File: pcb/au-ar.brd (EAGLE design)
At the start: 65 x 45 mm, 57 parts, among them U1 TPD12S016PWR, U2 TPD12S016PWR

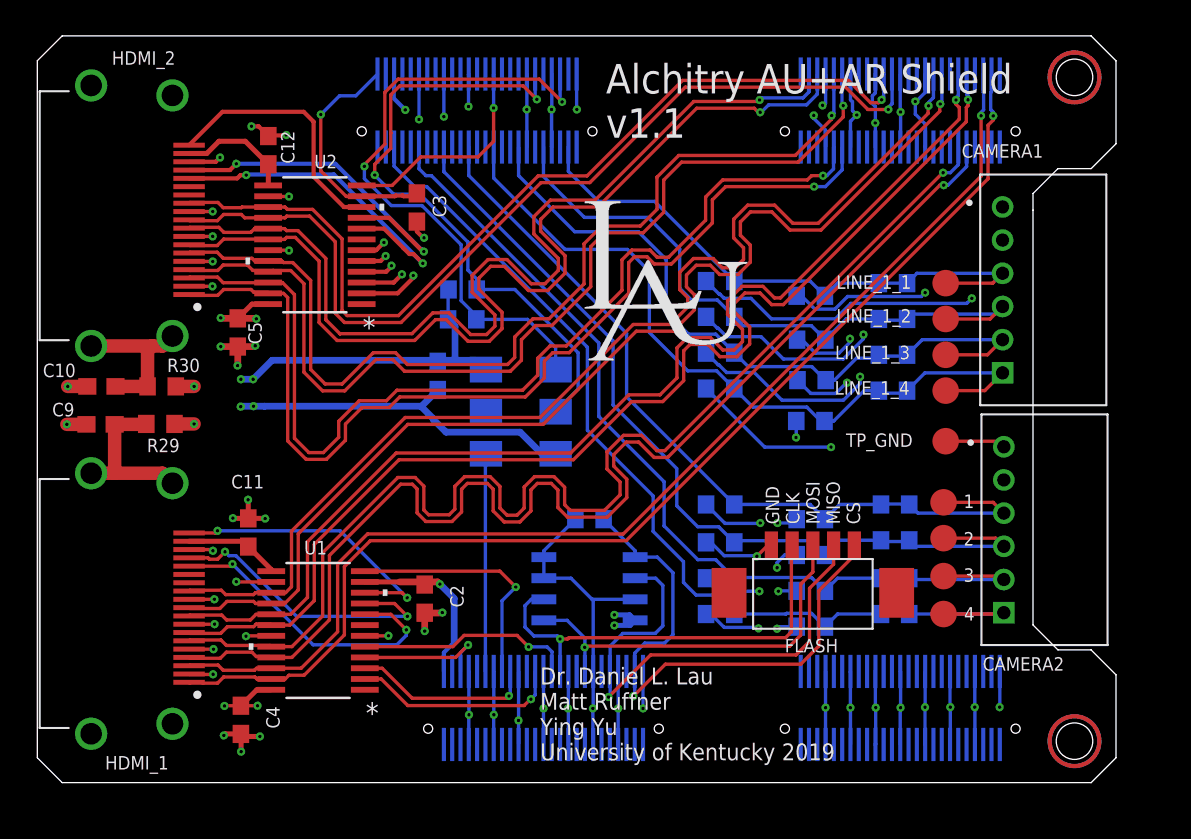
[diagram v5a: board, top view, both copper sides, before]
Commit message: retuned hdmi trace lengths, added ground pour and cutouts under hdmi connectors
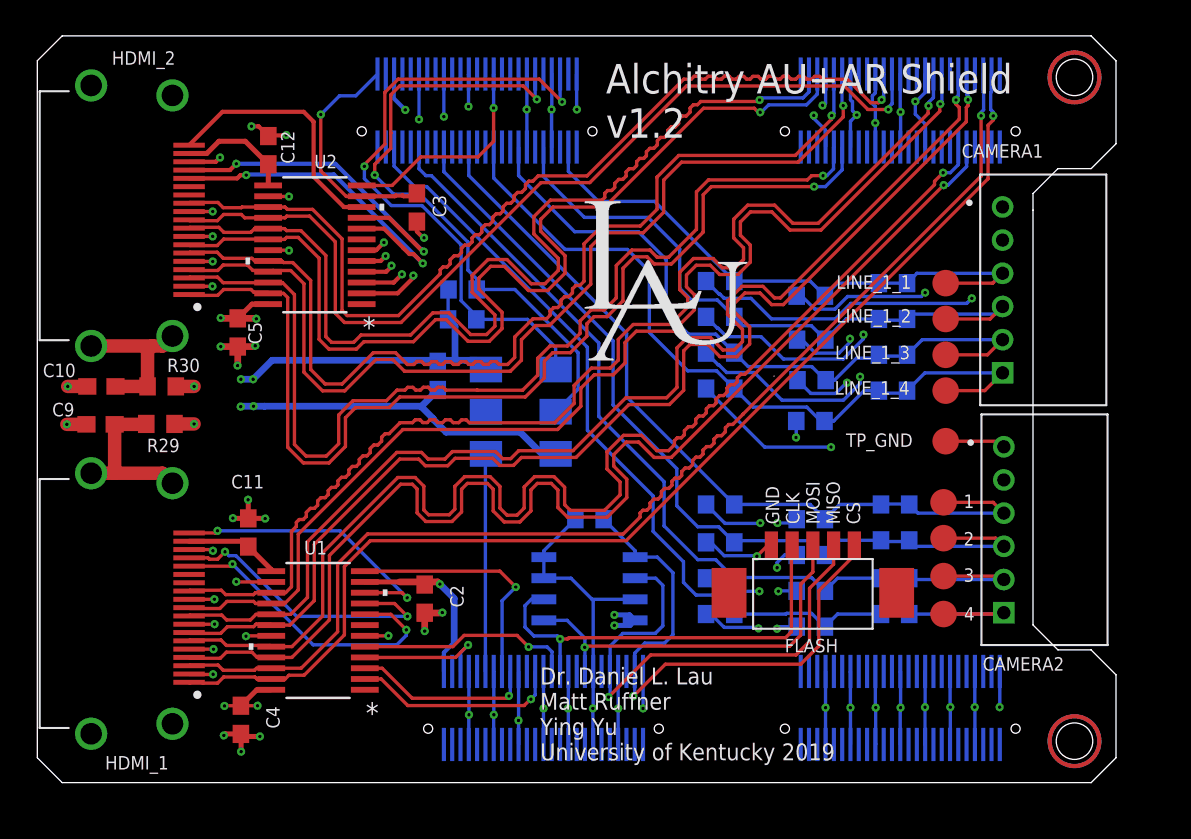
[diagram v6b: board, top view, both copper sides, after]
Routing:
- net CLK1_N: track 66.7 -> 70.0 mm
- net CLK2_N: track 55.3 -> 57.9 mm
- net D02_N: track 59.5 -> 61.9 mm
- net D22_N: track 60.1 -> 62.4 mm
- net D22_P: track 60.8 -> 62.7 mm
- net CLK1_P: track 67.6 -> 69.0 mm
- net D21_N: track 68.8 -> 70.1 mm
- net D12_N: track 58.5 -> 59.7 mm
- net D02_P: track 60.4 -> 61.6 mm
- net D11_N: track 74.6 -> 75.6 mm
- net D01_P: track 69.6 -> 70.6 mm
- net D01_N: track 68.9 -> 69.9 mm
- added copper zone on layer 2, net N$1
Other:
- board text added: "Alchitry AU+AR Shield v1.2"
- board text removed: "Alchitry AU+AR Shield v1.1"

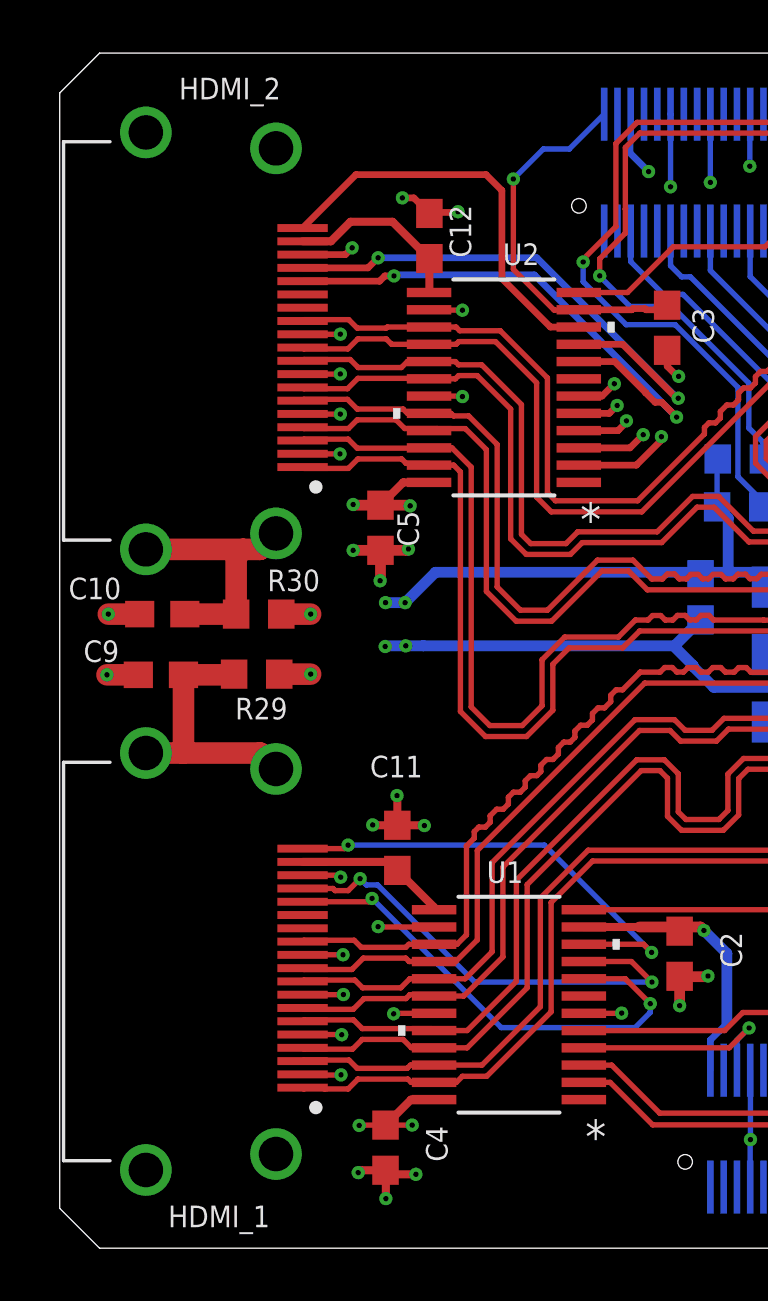
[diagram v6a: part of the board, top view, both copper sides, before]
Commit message: added partslist and solder jumper for hdmi input, labeled hdmi input and output added up to date gerbers.
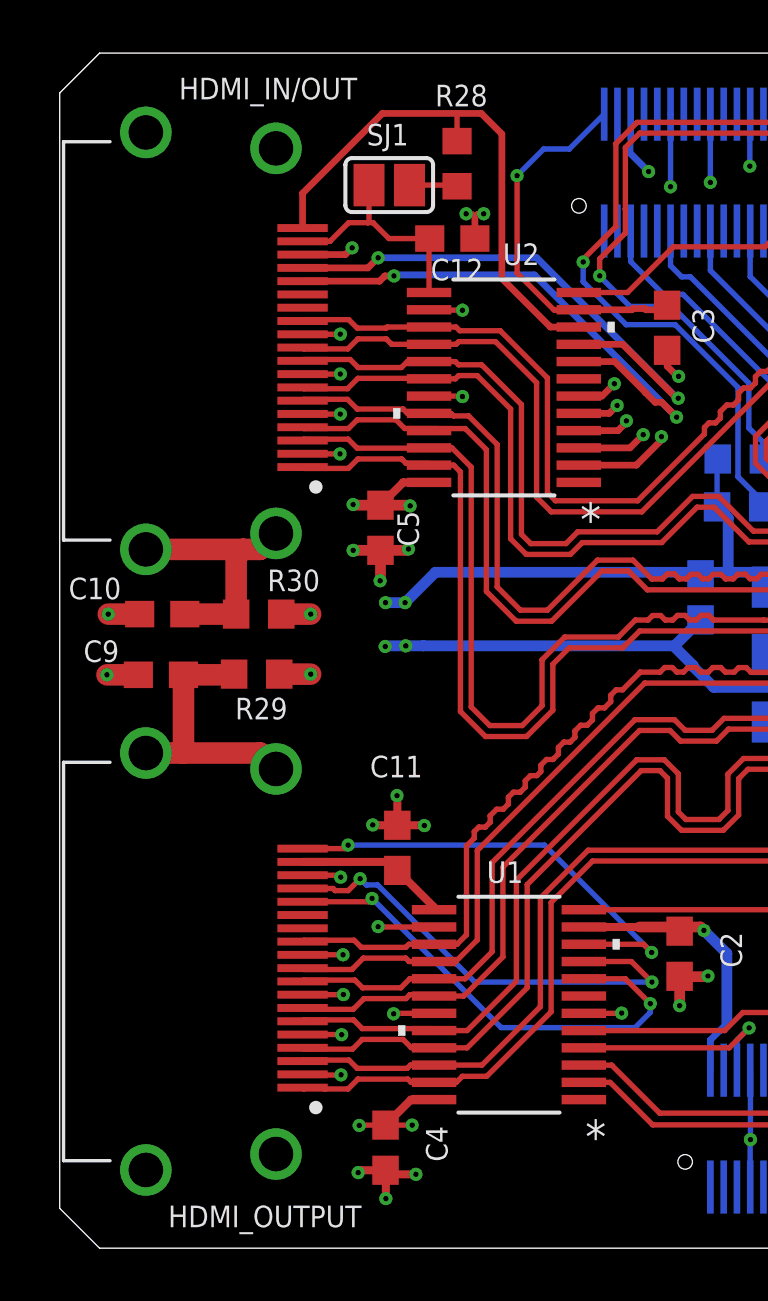
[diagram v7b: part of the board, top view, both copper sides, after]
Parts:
- added R28: 2k, rcl:R0603
- added SJ1: (no value), jumper:SJ
- R1, R10, R11, R12, R13, R14, R15, R16, R17, R18, R19, R2, R20, R21, R22, R23, R24, R25, R26, R3, R4, R7, R8, R9: value (none) -> DNP
- moved C12 0.87 mm to (14.8, 38.0), turned to 0 degrees
- renumbered HDMI_1 to HDMI_OUTPUT, HDMI_2 to HDMI_IN/OUT
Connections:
- new net N$2: R28.1, SJ1.1
- net 5VHDMI2: now also SJ1.2
- net HP2: now also R28.2
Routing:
- net HP2: track 15.6 -> 20.5 mm
- net 5VHDMI2: track 6.94 -> 8.82 mm
- net N$2: track 0.00 -> 1.81 mm
- net GND: track 200.5 -> 199.7 mm

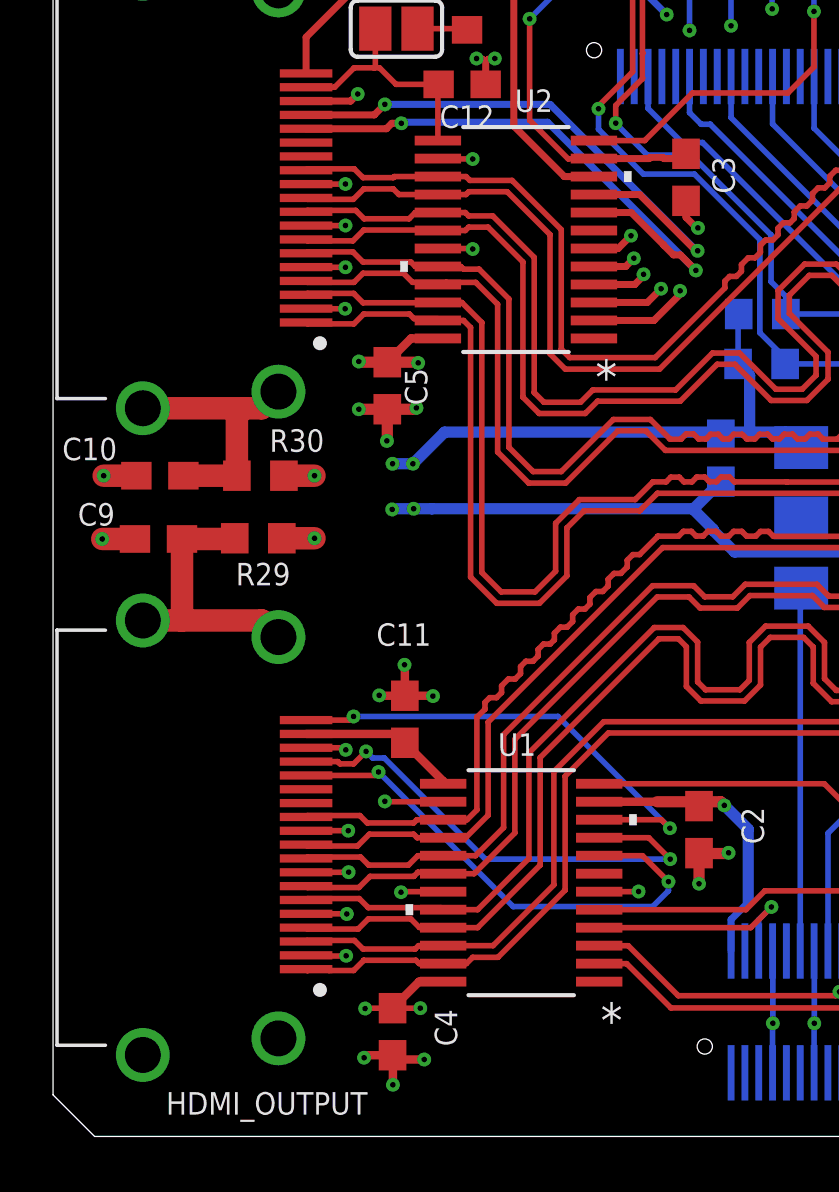
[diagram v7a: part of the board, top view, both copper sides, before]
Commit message: hdmi ground vias moved
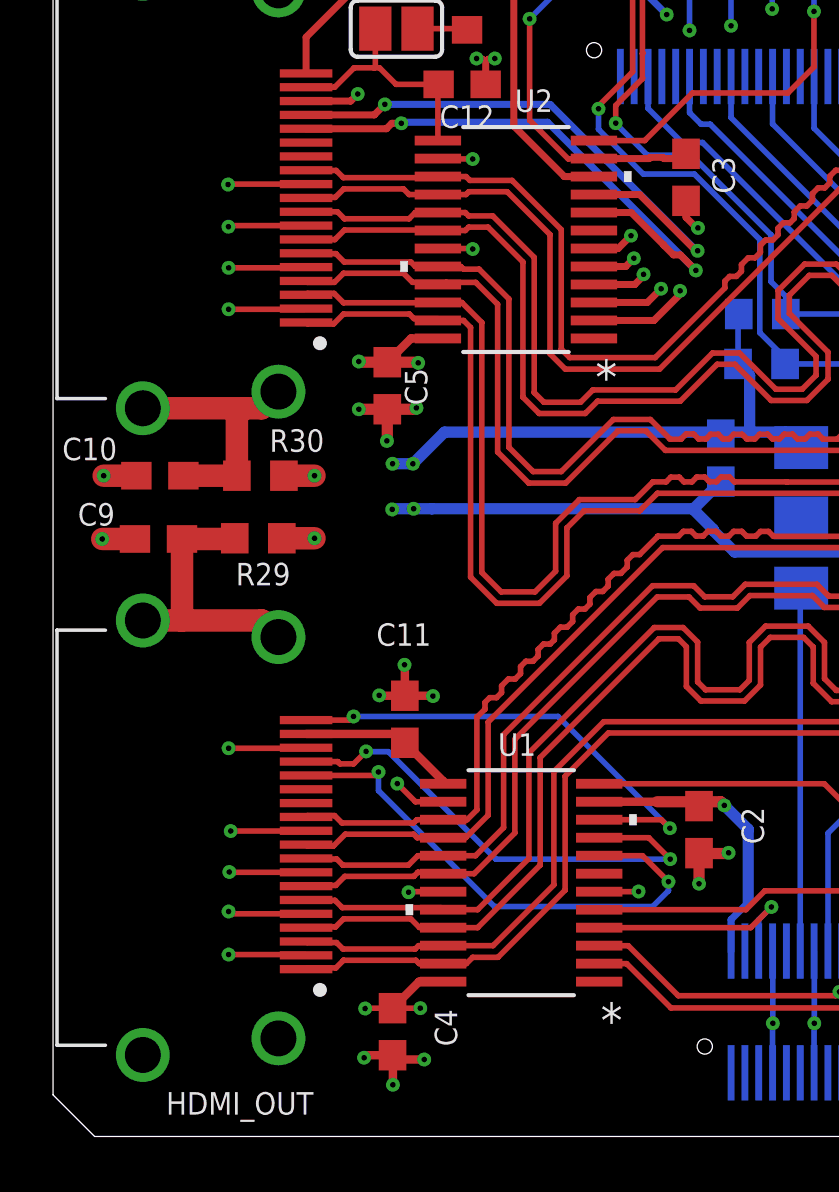
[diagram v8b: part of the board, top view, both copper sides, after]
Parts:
- renumbered HDMI_OUTPUT to HDMI_OUT
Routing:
- net GND: track 199.7 -> 211.4 mm
